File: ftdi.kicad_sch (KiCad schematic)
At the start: 10 parts, among them J2 Conn_01x06, U5 SN74AXC4T774RSV, U7 FT230XQ

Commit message: SDReWire: Footprint assigment
Signed-off-by: Dominik Sliwa <dominik@sliwa.io>
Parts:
- J2: footprint Connector_Molex:Molex_CLIK-Mate_502382-0670_1x06-1MP_P1.25mm_Vertical -> Connector_JST:JST_SH_SM06B-SRSS-TB_1x06-1MP_P1.00mm_Horizontal
- R12, RN2: footprint (none) -> Resistor_SMD:R_0402_1005Metric
- U5: footprint (none) -> Custom:QFN-16_1.8x2.6_Pitch0.4mm
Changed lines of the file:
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@@
       (effects (font (size 1.27 1.27)) (justify left))
     )
-    (property "Footprint" "" (id 2) (at 175.895 106.045 0)
+    (property "Footprint" "Resistor_SMD:R_0402_1005Metric" (id 2) (at 175.895 106.045 0)
       (effects (font (size 1.27 1.27)) hide)
     )
@@
       (effects (font (size 1.27 1.27)) (justify left))
     )
-    (property "Footprint" "Connector_Molex:Molex_CLIK-Mate_502382-0670_1x06-1MP_P1.25mm_Vertical" (id 2) (at 250.19 84.455 0)
+    (property "Footprint" "Connector_JST:JST_SH_SM06B-SRSS-TB_1x06-1MP_P1.00mm_Horizontal" (id 2) (at 250.19 84.455 0)
       (effects (font (size 1.27 1.27)) hide)
     )
@@
     (property "Reference" "RN2" (id 0) (at 224.155 75.565 90))
     (property "Value" "100" (id 1) (at 224.155 78.105 90))
-    (property "Footprint" "" (id 2) (at 224.155 77.47 90)
+    (property "Footprint" "Resistor_SMD:R_0402_1005Metric" (id 2) (at 224.155 77.47 90)
       (effects (font (size 1.27 1.27)) hide)
     )
@@
     (property "Reference" "U5" (id 0) (at 189.23 111.125 0))
     (property "Value" "SN74AXC4T774RSV" (id 1) (at 206.375 111.76 0))
-    (property "Footprint" "" (id 2) (at 198.755 76.835 0)
+    (property "Footprint" "Custom:QFN-16_1.8x2.6_Pitch0.4mm" (id 2) (at 198.755 76.835 0)
       (effects (font (size 1.27 1.27)) hide)
     )

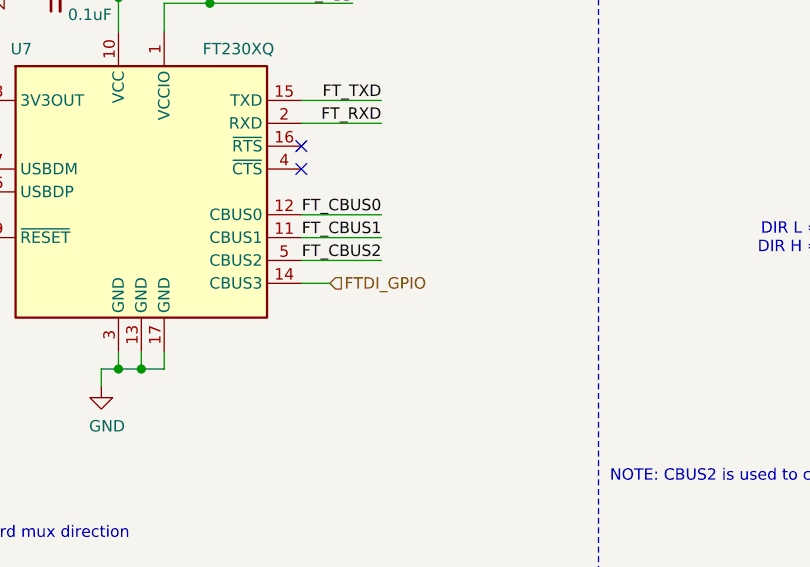
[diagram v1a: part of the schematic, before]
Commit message: SDReWire: rename FTDI_GPIO to SD_MUX_SEL and fix assigment
Resistor array had a wrong footprint

Signed-off-by: Dominik Sliwa <dominik@sliwa.io>
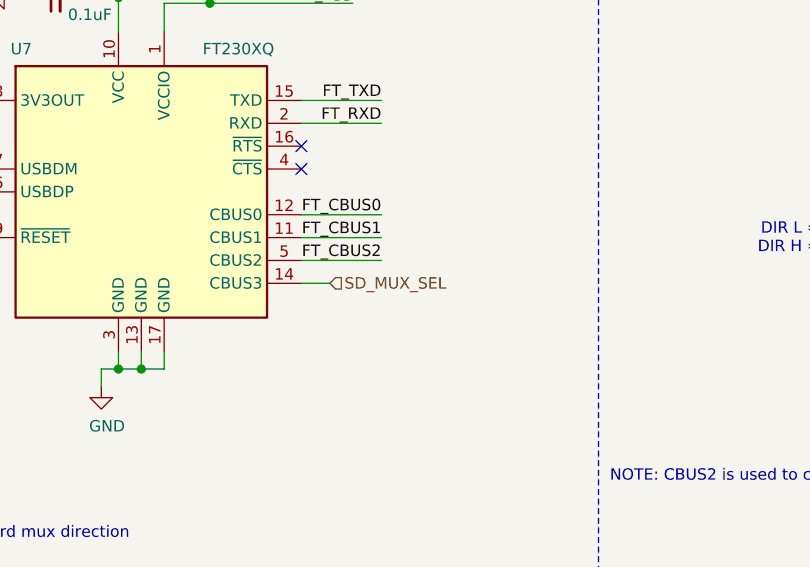
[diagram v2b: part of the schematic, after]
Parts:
- RN2: footprint Resistor_SMD:R_0402_1005Metric -> Resistor_SMD:R_Array_Convex_4x0402
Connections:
- net FTDI_GPIO renamed SD_MUX_SEL
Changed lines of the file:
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@@
     (effects (font (size 1.27 1.27)) (justify right))
   )
-  (hierarchical_label "FTDI_GPIO" (shape input) (at 106.68 104.775 0)
+  (hierarchical_label "SD_MUX_SEL" (shape input) (at 106.68 104.775 0)
     (effects (font (size 1.27 1.27)) (justify left))
   )
@@
     (property "Reference" "RN2" (id 0) (at 224.155 75.565 90))
     (property "Value" "100" (id 1) (at 224.155 78.105 90))
-    (property "Footprint" "Resistor_SMD:R_0402_1005Metric" (id 2) (at 224.155 77.47 90)
-      (effects (font (size 1.27 1.27)) hide)
-    )
+    (property "Footprint" "Resistor_SMD:R_Array_Convex_4x0402" (id 2) (at 224.155 77.47 90)
+      (effects (font (size 1.27 1.27)) hide)
+    )

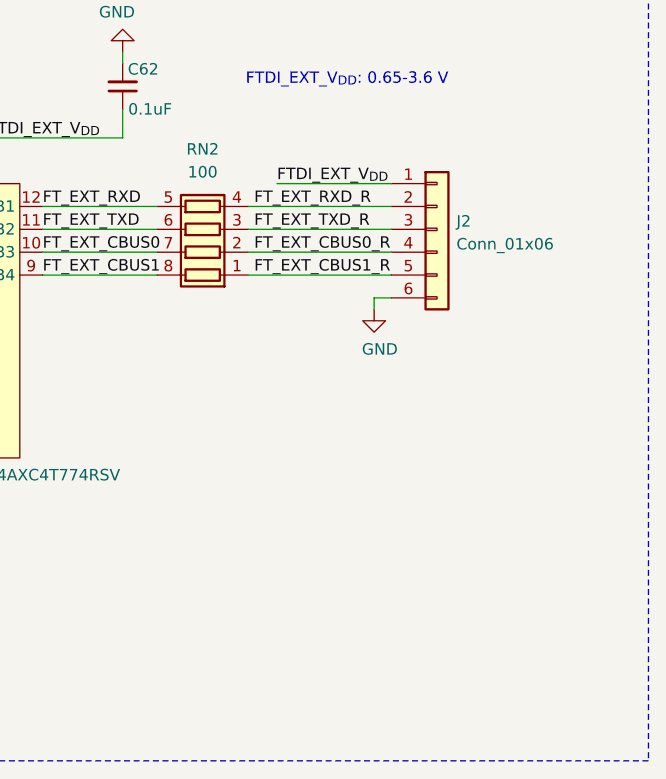
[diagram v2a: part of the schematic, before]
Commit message: SDReWire: fix assigments
modify few components footprint assigments

Signed-off-by: Dominik Sliwa <dominik@sliwa.io>
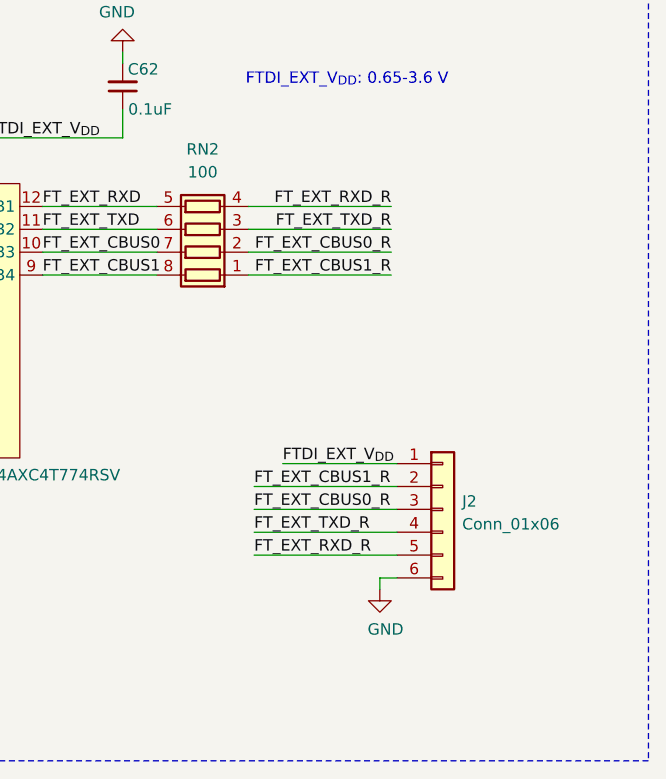
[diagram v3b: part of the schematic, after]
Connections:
- net FT_EXT_CBUS0_R: now also J2.3 (Pin_3); no longer J2.4 (Pin_4)
- net FT_EXT_CBUS1_R: now also J2.2 (Pin_2); no longer J2.5 (Pin_5)
- net FT_EXT_RXD_R: now also J2.5 (Pin_5); no longer J2.2 (Pin_2)
- net FT_EXT_TXD_R: now also J2.4 (Pin_4); no longer J2.3 (Pin_3)
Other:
- moved on the sheet: J2
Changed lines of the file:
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@@
     (stroke (width 0) (type solid) (color 0 0 0 0))
   )
-  (wire (pts (xy 232.41 79.375) (xy 245.11 79.375))
-    (stroke (width 0) (type solid) (color 0 0 0 0))
-  )
-  (wire (pts (xy 243.205 92.075) (xy 243.205 93.345))
-    (stroke (width 0) (type solid) (color 0 0 0 0))
-  )
-  (wire (pts (xy 245.11 92.075) (xy 243.205 92.075))
+  (wire (pts (xy 233.045 110.49) (xy 245.745 110.49))
+    (stroke (width 0) (type solid) (color 0 0 0 0))
+  )
+  (wire (pts (xy 243.84 123.19) (xy 243.84 124.46))
+    (stroke (width 0) (type solid) (color 0 0 0 0))
+  )
+  (wire (pts (xy 245.745 113.03) (xy 229.87 113.03))
+    (stroke (width 0) (type solid) (color 0 0 0 0))
+  )
+  (wire (pts (xy 245.745 115.57) (xy 229.87 115.57))
+    (stroke (width 0) (type solid) (color 0 0 0 0))
+  )
+  (wire (pts (xy 245.745 118.11) (xy 229.87 118.11))
+    (stroke (width 0) (type solid) (color 0 0 0 0))
+  )
+  (wire (pts (xy 245.745 120.65) (xy 229.87 120.65))
+    (stroke (width 0) (type solid) (color 0 0 0 0))
+  )
+  (wire (pts (xy 245.745 123.19) (xy 243.84 123.19))
     (stroke (width 0) (type solid) (color 0 0 0 0))
   )
@@
     (effects (font (size 1.27 1.27)) (justify right bottom))
   )
-  (label "FT_EXT_RXD_R" (at 229.87 81.915 0)
-    (effects (font (size 1.27 1.27)) (justify left bottom))
-  )
-  (label "FT_EXT_TXD_R" (at 229.87 84.455 0)
-    (effects (font (size 1.27 1.27)) (justify left bottom))
-  )
-  (label "FT_EXT_CBUS0_R" (at 229.87 86.995 0)
-    (effects (font (size 1.27 1.27)) (justify left bottom))
-  )
-  (label "FT_EXT_CBUS1_R" (at 229.87 89.535 0)
-    (effects (font (size 1.27 1.27)) (justify left bottom))
-  )
-  (label "FTDI_EXT_V_{DD}" (at 232.41 79.375 0)
-    (effects (font (size 1.27 1.27)) (justify left bottom))
+  (label "FT_EXT_CBUS1_R" (at 229.87 113.03 0)
+    (effects (font (size 1.27 1.27)) (justify left bottom))
+  )
+  (label "FT_EXT_CBUS0_R" (at 229.87 115.57 0)
+    (effects (font (size 1.27 1.27)) (justify left bottom))
+  )
+  (label "FT_EXT_TXD_R" (at 229.87 118.11 0)
+    (effects (font (size 1.27 1.27)) (justify left bottom))
+  )
+  (label "FT_EXT_RXD_R" (at 229.87 120.65 0)
+    (effects (font (size 1.27 1.27)) (justify left bottom))
+  )
+  (label "FTDI_EXT_V_{DD}" (at 233.045 110.49 0)
+    (effects (font (size 1.27 1.27)) (justify left bottom))
+  )
+  (label "FT_EXT_RXD_R" (at 245.11 81.915 180)
+    (effects (font (size 1.27 1.27)) (justify right bottom))
+  )
+  (label "FT_EXT_TXD_R" (at 245.11 84.455 180)
+    (effects (font (size 1.27 1.27)) (justify right bottom))
+  )
+  (label "FT_EXT_CBUS0_R" (at 245.11 86.995 180)
+    (effects (font (size 1.27 1.27)) (justify right bottom))
+  )
+  (label "FT_EXT_CBUS1_R" (at 245.11 89.535 180)
+    (effects (font (size 1.27 1.27)) (justify right bottom))
   )
   (hierarchical_label "FTDI_USB2_D-" (shape input) (at 64.135 92.075 180)
@@
     )
   )
-  (symbol (lib_id "power:GND") (at 243.205 93.345 0) (unit 1)
-    (in_bom yes) (on_board yes)
-    (property "Reference" "#PWR0154" (id 0) (at 243.205 99.695 0)
-      (effects (font (size 1.27 1.27)) hide)
-    )
-    (property "Value" "GND" (id 1) (at 243.84 97.79 0))
-    (property "Footprint" "" (id 2) (at 243.205 93.345 0)
-      (effects (font (size 1.27 1.27)) hide)
-    )
-    (property "Datasheet" "" (id 3) (at 243.205 93.345 0)
+  (symbol (lib_id "power:GND") (at 243.84 124.46 0) (unit 1)
+    (in_bom yes) (on_board yes)
+    (property "Reference" "#PWR0154" (id 0) (at 243.84 130.81 0)
+      (effects (font (size 1.27 1.27)) hide)
+    )
+    (property "Value" "GND" (id 1) (at 244.475 128.905 0))
+    (property "Footprint" "" (id 2) (at 243.84 124.46 0)
+      (effects (font (size 1.27 1.27)) hide)
+    )
+    (property "Datasheet" "" (id 3) (at 243.84 124.46 0)
       (effects (font (size 1.27 1.27)) hide)
     )
@@
     )
   )
-  (symbol (lib_id "Connector_Generic:Conn_01x06") (at 250.19 84.455 0) (unit 1)
-    (in_bom yes) (on_board yes)
-    (property "Reference" "J2" (id 0) (at 252.349 83.566 0)
+  (symbol (lib_id "Connector_Generic:Conn_01x06") (at 250.825 115.57 0) (unit 1)
+    (in_bom yes) (on_board yes)
+    (property "Reference" "J2" (id 0) (at 252.984 114.681 0)
       (effects (font (size 1.27 1.27)) (justify left))
     )
-    (property "Value" "Conn_01x06" (id 1) (at 252.349 86.106 0)
+    (property "Value" "Conn_01x06" (id 1) (at 252.984 117.221 0)
       (effects (font (size 1.27 1.27)) (justify left))
     )
-    (property "Footprint" "Connector_JST:JST_SH_SM06B-SRSS-TB_1x06-1MP_P1.00mm_Horizontal" (id 2) (at 250.19 84.455 0)
-      (effects (font (size 1.27 1.27)) hide)
-    )
-    (property "Datasheet" "~" (id 3) (at 250.19 84.455 0)
-      (effects (font (size 1.27 1.27)) hide)
-    )
+    (property "Footprint" "Connector_JST:JST_SH_SM06B-SRSS-TB_1x06-1MP_P1.00mm_Horizontal" (id 2) (at 250.825 115.57 0)
+      (effects (font (size 1.27 1.27)) hide)
+    )
+    (property "Datasheet" "~" (id 3) (at 250.825 115.57 0)
+      (effects (font (size 1.27 1.27)) hide)
+    )

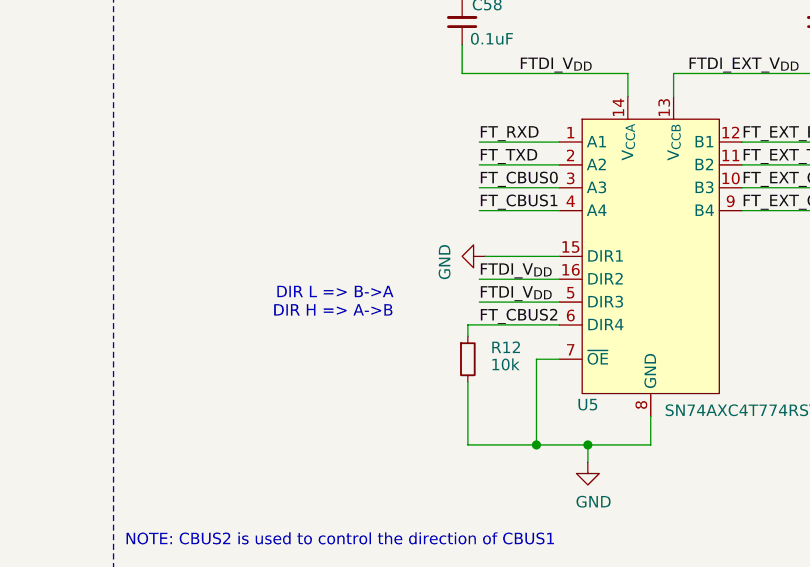
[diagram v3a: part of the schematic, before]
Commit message: SDReWire: add configurable link for gpio dir
Signed-off-by: Dominik Sliwa <dominik@sliwa.io>
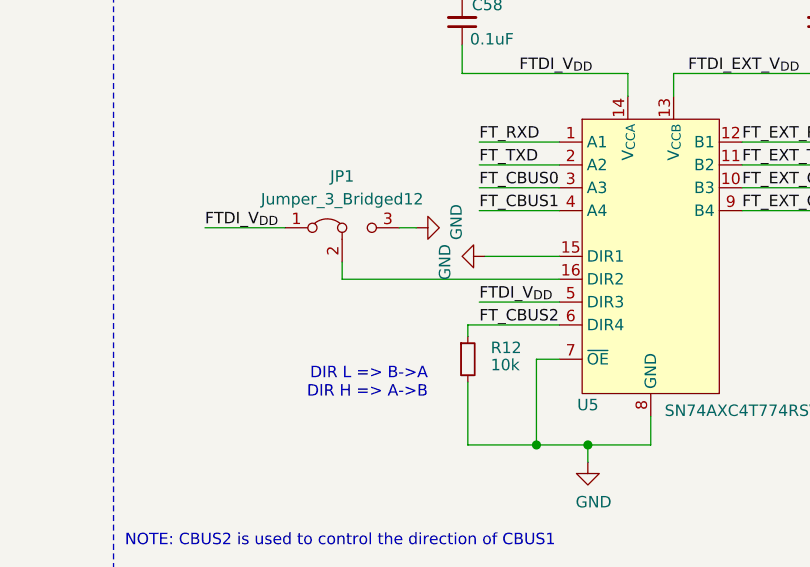
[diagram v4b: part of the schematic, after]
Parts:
- added JP1: Jumper_3_Bridged12, Jumper:SolderJumper-3_P1.3mm_Bridged12_RoundedPad1.0x1.5mm_NumberLabels, symbol Jumper:Jumper_3_Bridged12
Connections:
- net FTDI_V_{DD}: now also JP1.1 (A); no longer U5.16 (DIR2)
- net GND: now also JP1.3 (B)
- new net: JP1.2 (C), U5.16 (DIR2)
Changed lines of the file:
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@@
+    (stroke (width 0) (type solid) (color 0 0 0 0))
+  )
+  (wire (pts (xy 146.685 91.44) (xy 155.575 91.44))
+    (stroke (width 0) (type solid) (color 0 0 0 0))
+  )
+  (wire (pts (xy 161.925 97.155) (xy 161.925 95.25))
+    (stroke (width 0) (type solid) (color 0 0 0 0))
+  )
+  (wire (pts (xy 168.275 91.44) (xy 170.18 91.44))
     (stroke (width 0) (type solid) (color 0 0 0 0))
   )
@@
     (stroke (width 0) (type solid) (color 0 0 0 0))
   )
-  (wire (pts (xy 177.165 97.155) (xy 186.055 97.155))
-    (stroke (width 0) (type solid) (color 0 0 0 0))
-  )
   (wire (pts (xy 177.165 99.695) (xy 186.055 99.695))
     (stroke (width 0) (type solid) (color 0 0 0 0))
@@
   )
   (wire (pts (xy 186.055 89.535) (xy 177.165 89.535))
+    (stroke (width 0) (type solid) (color 0 0 0 0))
+  )
+  (wire (pts (xy 186.055 97.155) (xy 161.925 97.155))
     (stroke (width 0) (type solid) (color 0 0 0 0))
   )
@@
     (effects (font (size 1.27 1.27)) (justify left bottom))
   )
-  (text "DIR L => B->A\nDIR H => A->B" (at 167.64 101.6 180)
+  (text "DIR L => B->A\nDIR H => A->B" (at 171.45 110.49 180)
     (effects (font (size 1.27 1.27)) (justify right bottom))
   )
@@
     (effects (font (size 1.27 1.27)) (justify right bottom))
   )
+  (label "FTDI_V_{DD}" (at 146.685 91.44 0)
+    (effects (font (size 1.27 1.27)) (justify left bottom))
+  )
   (label "FT_RXD" (at 177.165 81.915 0)
     (effects (font (size 1.27 1.27)) (justify left bottom))
@@
   )
   (label "FT_CBUS1" (at 177.165 89.535 0)
-    (effects (font (size 1.27 1.27)) (justify left bottom))
-  )
-  (label "FTDI_V_{DD}" (at 177.165 97.155 0)
     (effects (font (size 1.27 1.27)) (justify left bottom))
   )
@@
     )
     (property "Datasheet" "" (id 3) (at 93.345 62.23 0)
+      (effects (font (size 1.27 1.27)) hide)
+    )
+  )
+  (symbol (lib_id "power:GND") (at 170.18 91.44 90) (unit 1)
+    (in_bom yes) (on_board yes)
+    (property "Reference" "#PWR026" (id 0) (at 176.53 91.44 0)
+      (effects (font (size 1.27 1.27)) hide)
+    )
+    (property "Value" "GND" (id 1) (at 174.625 90.805 0))
+    (property "Footprint" "" (id 2) (at 170.18 91.44 0)
+      (effects (font (size 1.27 1.27)) hide)
+    )
+    (property "Datasheet" "" (id 3) (at 170.18 91.44 0)
       (effects (font (size 1.27 1.27)) hide)
     )
@@
       (effects (font (size 1.27 1.27)) hide)
     )
+  )
+  (symbol (lib_id "Jumper:Jumper_3_Bridged12") (at 161.925 91.44 0) (unit 1)
+    (in_bom yes) (on_board yes)
+    (property "Reference" "JP1" (id 0) (at 161.925 85.725 0))
+    (property "Value" "Jumper_3_Bridged12" (id 1) (at 161.925 88.265 0))
+    (property "Footprint" "Jumper:SolderJumper-3_P1.3mm_Bridged12_RoundedPad1.0x1.5mm_NumberLabels" (id 2) (at 161.925 91.44 0)
+      (effects (font (size 1.27 1.27)) hide)
+    )
+    (property "Datasheet" "~" (id 3) (at 161.925 91.44 0)
+      (effects (font (size 1.27 1.27)) hide)
+    )

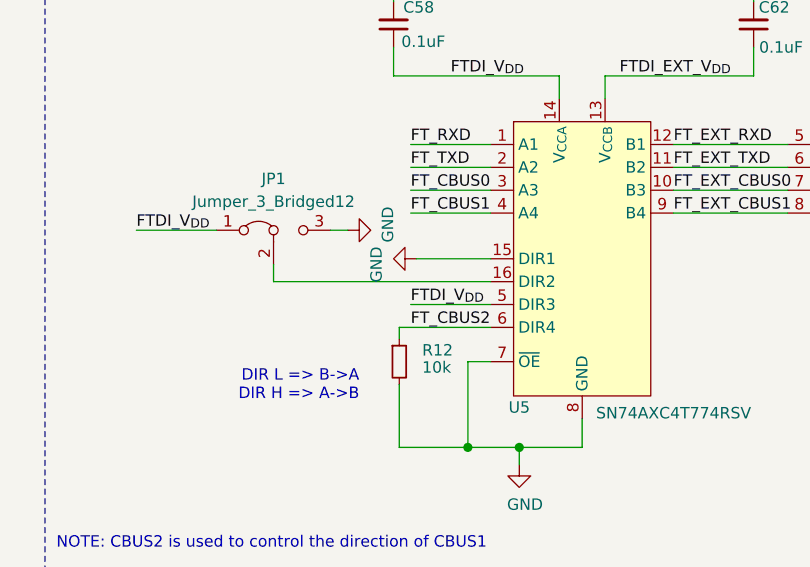
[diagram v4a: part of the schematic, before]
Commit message: sd.kicad_sch: improve SD_MUX_SEL net readability
Signed-off-by: Dominik Sliwa <dominik@sliwa.io>
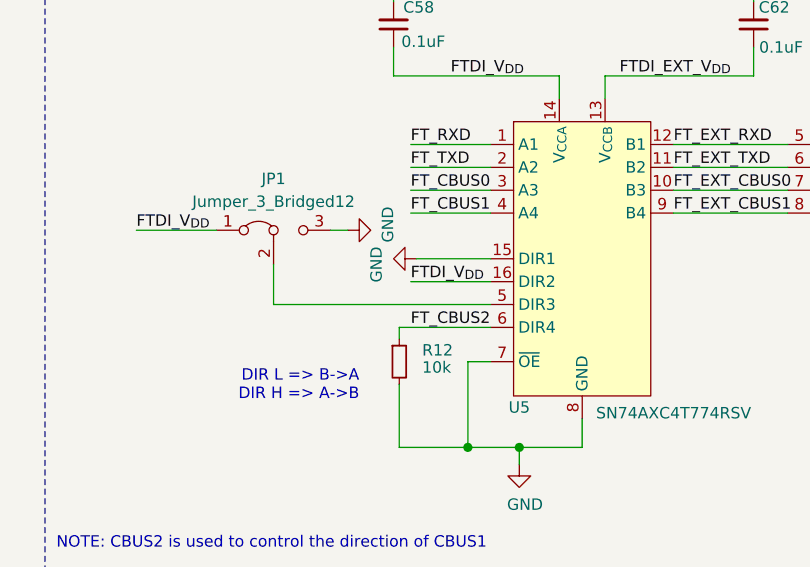
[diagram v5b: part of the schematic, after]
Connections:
- net FTDI_V_{DD}: now also U5.16 (DIR2); no longer U5.5 (DIR3)
- net at JP1.2 (C): now also U5.5 (DIR3); no longer U5.16 (DIR2)
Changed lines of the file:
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@@
     (stroke (width 0) (type solid) (color 0 0 0 0))
   )
-  (wire (pts (xy 161.925 97.155) (xy 161.925 95.25))
+  (wire (pts (xy 161.925 95.25) (xy 161.925 99.695))
     (stroke (width 0) (type solid) (color 0 0 0 0))
   )
@@
     (stroke (width 0) (type solid) (color 0 0 0 0))
   )
-  (wire (pts (xy 177.165 99.695) (xy 186.055 99.695))
+  (wire (pts (xy 177.165 97.155) (xy 186.055 97.155))
     (stroke (width 0) (type solid) (color 0 0 0 0))
   )
@@
     (stroke (width 0) (type solid) (color 0 0 0 0))
   )
-  (wire (pts (xy 186.055 97.155) (xy 161.925 97.155))
+  (wire (pts (xy 186.055 99.695) (xy 161.925 99.695))
     (stroke (width 0) (type solid) (color 0 0 0 0))
   )
@@
     (effects (font (size 1.27 1.27)) (justify left bottom))
   )
-  (label "FTDI_V_{DD}" (at 177.165 99.695 0)
-    (effects (font (size 1.27 1.27)) (justify left bottom))
-  )
+  (label "FTDI_V_{DD}" (at 177.165 97.155 0)
+    (effects (font (size 1.27 1.27)) (justify left bottom))
+  )
